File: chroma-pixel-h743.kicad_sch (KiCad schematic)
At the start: 4 parts

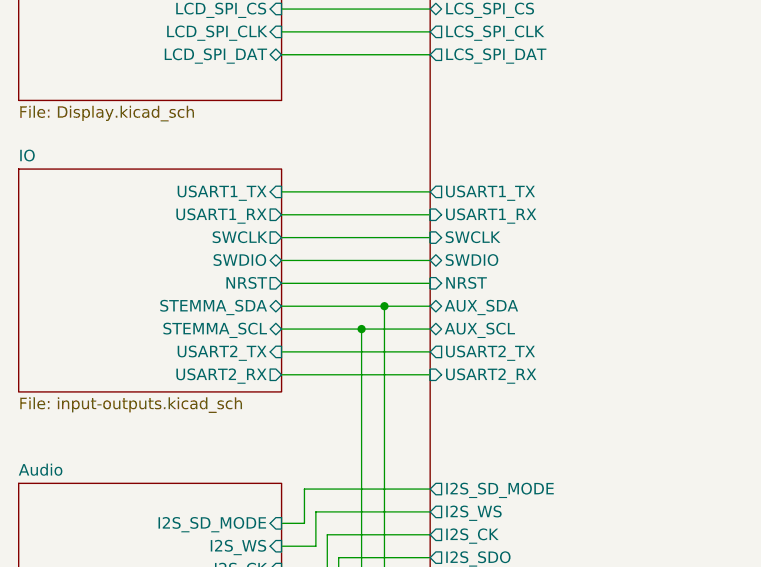
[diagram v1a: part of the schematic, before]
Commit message: Added chroma pixel png
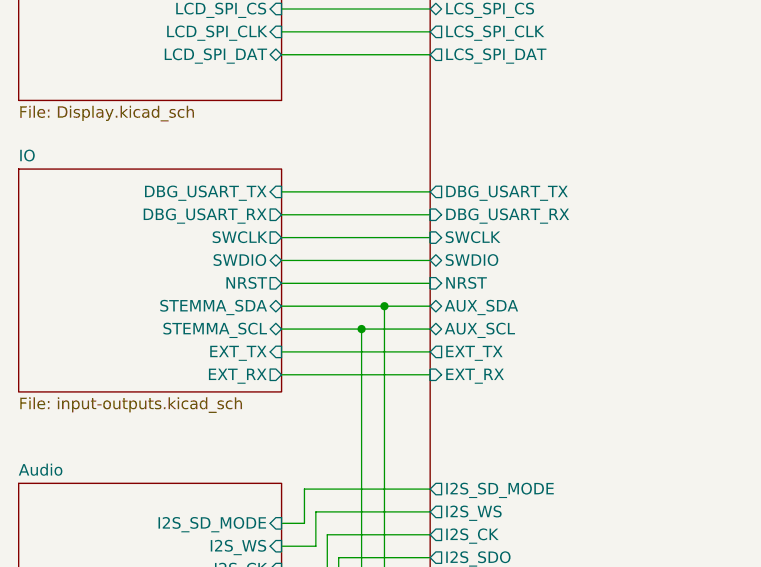
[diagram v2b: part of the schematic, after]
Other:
- sheet IO ports: added DBG_USART_RX, DBG_USART_TX, EXT_RX, EXT_TX; removed USART1_RX, USART1_TX, USART2_RX, USART2_TX
- sheet MCU ports: added DBG_USART_RX, DBG_USART_TX, EXT_RX, EXT_TX; removed USART1_RX, USART1_TX, USART2_RX, USART2_TX
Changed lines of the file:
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@@
-			)
-		)
-		(pin "USART1_TX" output
-			(at 104.14 87.63 180)
-			(effects
-				(font
-					(size 1.27 1.27)
-				)
-				(justify left)
-			)
-		)
-		(pin "USART1_RX" input
-			(at 104.14 90.17 180)
-			(effects
-				(font
-					(size 1.27 1.27)
-				)
-				(justify left)
 			)
 		)
@@
 			)
 		)
-		(pin "USART2_TX" output
-			(at 104.14 105.41 180)
-			(effects
-				(font
-					(size 1.27 1.27)
-				)
-				(justify left)
-			)
-		)
-		(pin "USART2_RX" input
-			(at 104.14 107.95 180)
-			(effects
-				(font
-					(size 1.27 1.27)
-				)
-				(justify left)
-			)
-		)
 		(pin "SDRAM_ADD[0..12]" output
 			(at 154.94 39.37 0)
@@
 				)
 				(justify right)
+			)
+		)
+		(pin "DBG_USART_TX" output
+			(at 104.14 87.63 180)
+			(effects
+				(font
+					(size 1.27 1.27)
+				)
+				(justify left)
+			)
+		)
+		(pin "DBG_USART_RX" input
+			(at 104.14 90.17 180)
+			(effects
+				(font
+					(size 1.27 1.27)
+				)
+				(justify left)
+			)
+		)
+		(pin "EXT_TX" output
+			(at 104.14 105.41 180)
+			(effects
+				(font
+					(size 1.27 1.27)
+				)
+				(justify left)
+			)
+		)
+		(pin "EXT_RX" input
+			(at 104.14 107.95 180)
+			(effects
+				(font
+					(size 1.27 1.27)
+				)
+				(justify left)
 			)
 		)
@@
 			)
 		)
-		(pin "USART1_TX" input
+		(pin "DBG_USART_RX" output
+			(at 87.63 90.17 0)
+			(effects
+				(font
+					(size 1.27 1.27)
+				)
+				(justify right)
+			)
+		)
+		(pin "DBG_USART_TX" input
 			(at 87.63 87.63 0)
 			(effects
@@
 			)
 		)
-		(pin "USART1_RX" output
-			(at 87.63 90.17 0)
-			(effects
-				(font
-					(size 1.27 1.27)
-				)
-				(justify right)
-			)
-		)
-		(pin "USART2_TX" input
+		(pin "EXT_RX" output
+			(at 87.63 107.95 0)
+			(effects
+				(font
+					(size 1.27 1.27)
+				)
+				(justify right)
+			)
+		)
+		(pin "EXT_TX" input
 			(at 87.63 105.41 0)
 			(effects
 				(font
-					(size 1.27 1.27)
-				)
-				(justify right)
-			)
-		)
-		(pin "USART2_RX" output
-			(at 87.63 107.95 0)
-			(effects
-				(font
